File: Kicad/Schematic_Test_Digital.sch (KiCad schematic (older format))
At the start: 72 parts, among them J301 GPS - I2C OUT, J302 SCREEN - I2C OUT, J303 SWD_DEBUG, J304 CONN_JOYSTICK, J305 GENERAL - I2C OUT, SW301 RESET PUSH, U301 TSX-3225, U302 MMC5603NJ, U303 LSM6DS33TR, U304 74HC595PW, U305 74HC595PW, U306 74HC595PW

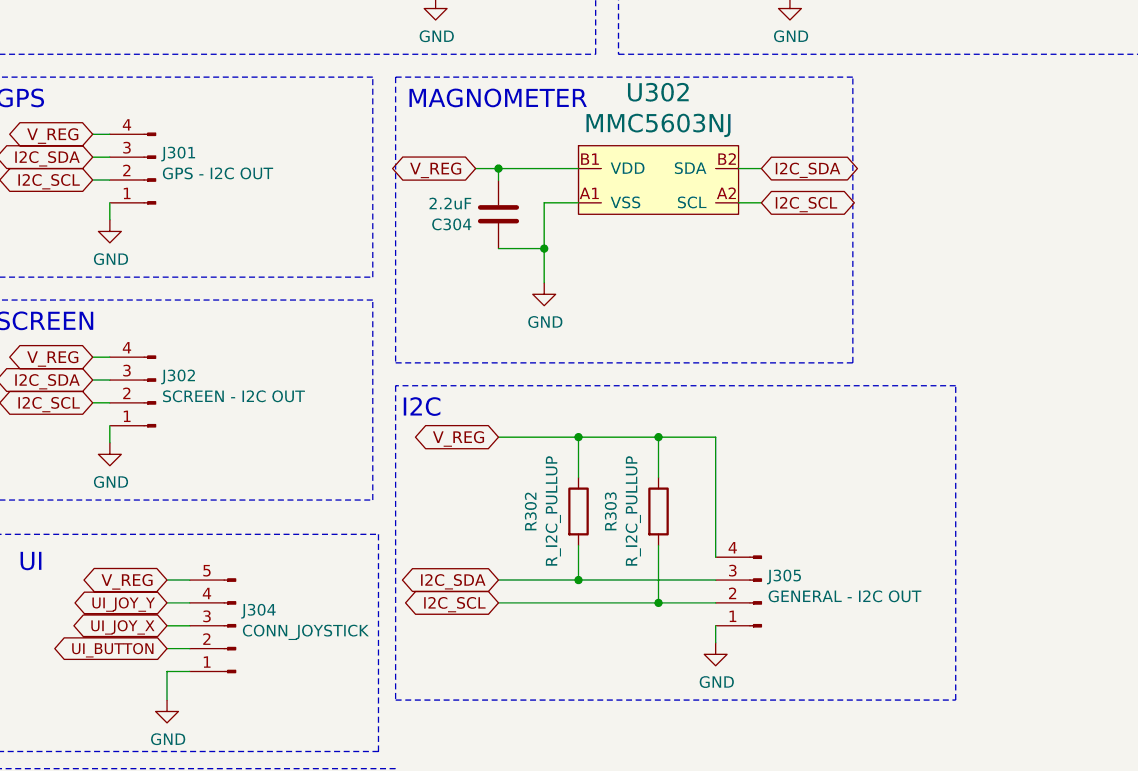
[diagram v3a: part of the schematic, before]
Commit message: "PREVIOUS COMMIT MAIN SCHEMATIC CORRUPTED (???).  Used commit before that."
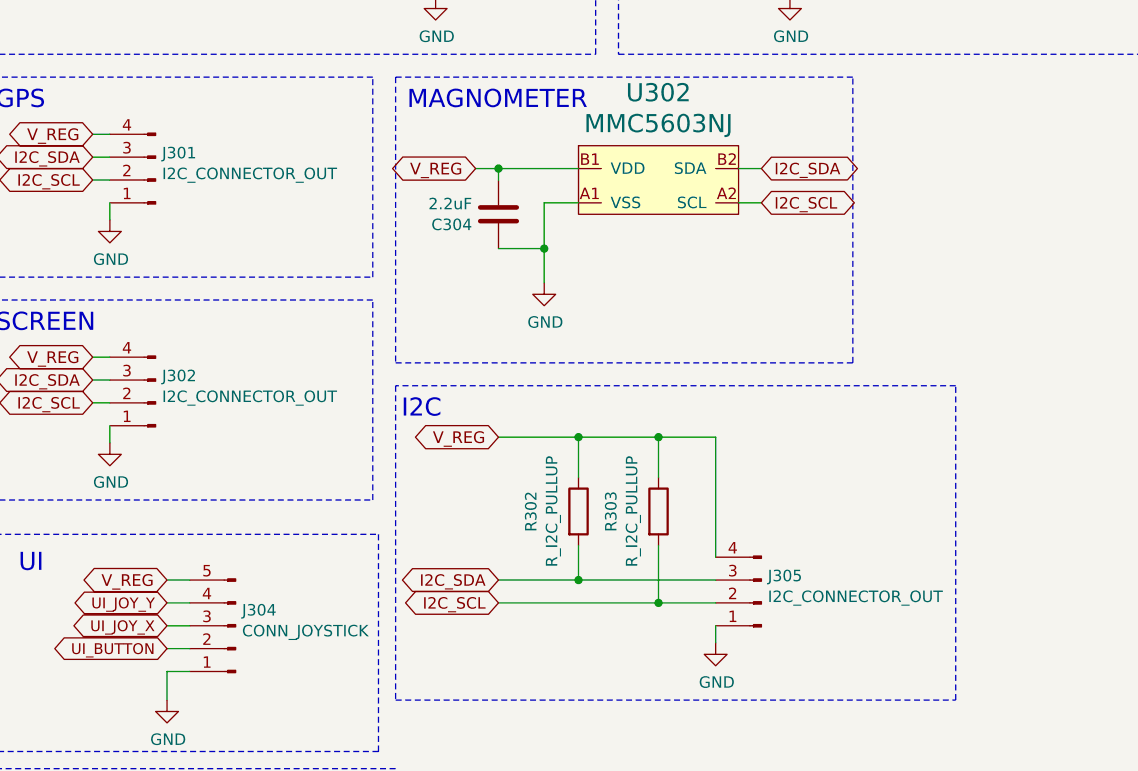
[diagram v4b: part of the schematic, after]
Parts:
- J301: value GPS - I2C OUT -> I2C_CONNECTOR_OUT; part_url (none) -> LOCAL STOCK
- J302: value SCREEN - I2C OUT -> I2C_CONNECTOR_OUT; part_url (none) -> LOCAL STOCK
- J305: value GENERAL - I2C OUT -> I2C_CONNECTOR_OUT; part_url (none) -> LOCAL STOCK
- U304, U305, U306: footprint Package_SO:TSSOP-16_4.4x5mm_P0.65mm -> Package_SO:TSSOP-14_4.4x5mm_P0.65mm
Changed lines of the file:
@@
 AR Path="/5F580392/5F64B2DD" Ref="J302"  Part="1"
 F 0 "J302" H 1272 4932 50  0000 R CNN
-F 1 "SCREEN - I2C OUT" H 1272 5023 50  0000 R CNN
+F 1 "I2C_CONNECTOR_OUT" H 1272 5023 50  0000 R CNN
 F 2 "Connector_JST:JST_EH_B4B-EH-A_1x04_P2.50mm_Vertical" H 1300 5050 50  0001 C CNN
 F 3 "~" H 1300 5050 50  0001 C CNN
 F 4 "JST - 4 pin" H 1300 5050 50  0001 C CNN "part_details"
-F 5 "" H 1300 5050 50  0001 C CNN "part_url"
+F 5 "LOCAL STOCK" H 1300 5050 50  0001 C CNN "part_url"
 	1    1300 5050
 	-1   0    0    1
@@
 AR Path="/5F580392/5F64B2F5" Ref="J301"  Part="1"
 F 0 "J301" H 1272 3957 50  0000 R CNN
-F 1 "GPS - I2C OUT" H 1272 4048 50  0000 R CNN
+F 1 "I2C_CONNECTOR_OUT" H 1272 4048 50  0000 R CNN
 F 2 "Connector_JST:JST_EH_B4B-EH-A_1x04_P2.50mm_Vertical" H 1300 4075 50  0001 C CNN
 F 3 "~" H 1300 4075 50  0001 C CNN
 F 4 "JST - 4 pin" H 1300 4075 50  0001 C CNN "part_details"
-F 5 "" H 1300 4075 50  0001 C CNN "part_url"
+F 5 "LOCAL STOCK" H 1300 4075 50  0001 C CNN "part_url"
 	1    1300 4075
 	-1   0    0    1
@@
 	0    1    1    0
 $EndComp
+Wire Wire Line
+	9550 4200 9900 4200
 Connection ~ 10700 3375
 Wire Wire Line
@@
 AR Path="/5F580392/5F64B4A9" Ref="J305"  Part="1"
 F 0 "J305" H 3922 5807 50  0000 R CNN
-F 1 "GENERAL - I2C OUT" H 3922 5898 50  0000 R CNN
+F 1 "I2C_CONNECTOR_OUT" H 3922 5898 50  0000 R CNN
 F 2 "Connector_JST:JST_EH_B4B-EH-A_1x04_P2.50mm_Vertical" H 3950 5925 50  0001 C CNN
 F 3 "~" H 3950 5925 50  0001 C CNN
 F 4 "JST - 4 pin" H 3950 5925 50  0001 C CNN "part_details"
-F 5 "" H 3950 5925 50  0001 C CNN "part_url"
+F 5 "LOCAL STOCK" H 3950 5925 50  0001 C CNN "part_url"
 	1    3950 5925
 	-1   0    0    1
@@
 	3000 4375 3000 4525
 Connection ~ 3000 4375
+Wire Wire Line
+	2800 4025 3150 4025
+Connection ~ 2800 4025
 Wire Wire Line
 	2700 4025 2800 4025
@@
 	1    0    0    -1
 $EndComp
+Wire Wire Line
+	3150 4175 3000 4175
+Wire Wire Line
+	3950 4175 3850 4175
+Wire Wire Line
+	3950 4025 3850 4025
 $Comp
 L StarGazer:MMC5603NJ U?
@@
 F 0 "U304" H 9125 1092 50  0000 C CNN
 F 1 "74HC595PW" H 9125 1000 51  0000 C CNN
-F 2 "Package_SO:TSSOP-16_4.4x5mm_P0.65mm" H 9200 1125 50  0001 C CNN
+F 2 "Package_SO:TSSOP-14_4.4x5mm_P0.65mm" H 9200 1125 50  0001 C CNN
 F 3 "" H 9200 1125 50  0001 C CNN
 F 4 "Shift Register" H 9150 1025 50  0001 C CNN "part_details"
@@
 F 0 "U306" H 9125 4067 50  0000 C CNN
 F 1 "74HC595PW" H 9125 3975 51  0000 C CNN
-F 2 "Package_SO:TSSOP-16_4.4x5mm_P0.65mm" H 9200 4100 50  0001 C CNN
+F 2 "Package_SO:TSSOP-14_4.4x5mm_P0.65mm" H 9200 4100 50  0001 C CNN
 F 3 "" H 9200 4100 50  0001 C CNN
 F 4 "Shift Register" H 9150 4000 50  0001 C CNN "part_details"
@@
 F 0 "U305" H 9125 2542 50  0000 C CNN
 F 1 "74HC595PW" H 9125 2450 51  0000 C CNN
-F 2 "Package_SO:TSSOP-16_4.4x5mm_P0.65mm" H 9200 2575 50  0001 C CNN
+F 2 "Package_SO:TSSOP-14_4.4x5mm_P0.65mm" H 9200 2575 50  0001 C CNN
 F 3 "" H 9200 2575 50  0001 C CNN
 F 4 "Shift Register" H 9150 2475 50  0001 C CNN "part_details"
@@
 Text Notes 650  6775 0    50   ~ 0
 SWD - PROGRAM\n
-Wire Wire Line
-	9550 4200 9900 4200
-Wire Wire Line
-	2800 4025 3150 4025
-Connection ~ 2800 4025
-Wire Wire Line
-	3000 4175 3150 4175
-Wire Wire Line
-	3950 4175 3850 4175
-Wire Wire Line
-	3850 4025 3950 4025
 $EndSCHEMATC

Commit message: End of night, progress continues.
Parts are getting initial placement.

confidence raises.
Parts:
- U304, U305, U306: footprint Package_SO:TSSOP-14_4.4x5mm_P0.65mm -> Package_SO:TSSOP-16_4.4x5mm_P0.65mm
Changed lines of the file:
@@
 F 0 "U304" H 9125 1092 50  0000 C CNN
 F 1 "74HC595PW" H 9125 1000 51  0000 C CNN
-F 2 "Package_SO:TSSOP-14_4.4x5mm_P0.65mm" H 9200 1125 50  0001 C CNN
+F 2 "Package_SO:TSSOP-16_4.4x5mm_P0.65mm" H 9200 1125 50  0001 C CNN
 F 3 "" H 9200 1125 50  0001 C CNN
 F 4 "Shift Register" H 9150 1025 50  0001 C CNN "part_details"
@@
 F 0 "U306" H 9125 4067 50  0000 C CNN
 F 1 "74HC595PW" H 9125 3975 51  0000 C CNN
-F 2 "Package_SO:TSSOP-14_4.4x5mm_P0.65mm" H 9200 4100 50  0001 C CNN
+F 2 "Package_SO:TSSOP-16_4.4x5mm_P0.65mm" H 9200 4100 50  0001 C CNN
 F 3 "" H 9200 4100 50  0001 C CNN
 F 4 "Shift Register" H 9150 4000 50  0001 C CNN "part_details"
@@
 F 0 "U305" H 9125 2542 50  0000 C CNN
 F 1 "74HC595PW" H 9125 2450 51  0000 C CNN
-F 2 "Package_SO:TSSOP-14_4.4x5mm_P0.65mm" H 9200 2575 50  0001 C CNN
+F 2 "Package_SO:TSSOP-16_4.4x5mm_P0.65mm" H 9200 2575 50  0001 C CNN
 F 3 "" H 9200 2575 50  0001 C CNN
 F 4 "Shift Register" H 9150 2475 50  0001 C CNN "part_details"

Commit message: Updated magnometer to LIS3MDL which has a more sane footprint.
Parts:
- added C309: 100nF, Capacitor_SMD:C_0805_2012Metric_Pad1.15x1.40mm_HandSolder, symbol Device:C
- added C310: 1uF, Capacitor_SMD:CP_Elec_4x3, symbol Device:CP
- C304: value 2.2uF -> 100nF
- U302: value MMC5603NJ -> LIS3MDLTR; footprint Package_BGA:WLP-4_0.73x0.73mm_Layout2x2_P0.35mm_Ball0.22mm_Pad0.2mm_NSMD -> Package_LGA:LGA-12_2x2mm_P0.5mm; symbol StarGazer:MMC5603NJ -> StarGazer:LIS3MDL; part_name MMC5603NJ -> LIS3MDLTR; part_url https://www.digikey.com/product-detail/en/memsic-inc/MMC560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 -> https://www.digikey.com/product-detail/en/stmicroelectronic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
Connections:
- net GND: now also C304.1, U302.12 (RES), U302.2 (RES), U302.3 (GND), C309.1, C310.2; no longer C304.2, U302.A1 (VSS)
- net I2C_SCL: now also U302.1 (SCL/SPC); no longer U302.A2 (SCL)
- net I2C_SDA: now also U302.11 (SDA/SDI/SDO); no longer U302.B2 (SDA)
- net V_REG: now also U302.10 (CS), U302.5 (VDD), U302.6 (VDD_IO), U302.9 (SD0/SA1), C309.2, C310.1; no longer C304.1, U302.B1 (VDD)
- new net: C304.2, U302.4 (C1)
- no-connect marks 3 -> 5

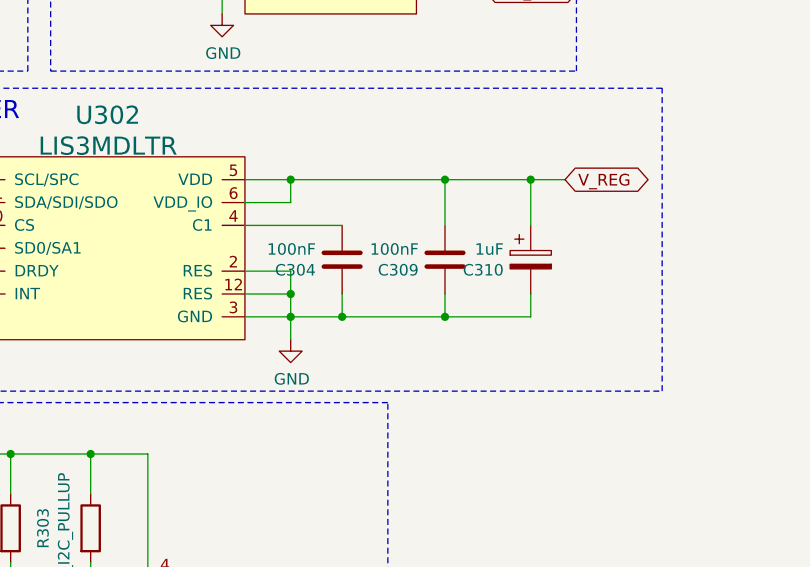
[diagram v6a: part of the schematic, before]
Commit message: Discovered small bug with BoM script.  It does not acccount for all parameters, such as foot print.  This resulted in it thinking a electro-cap could be a ceramic-cap since they shared the same value.
To simplify parts, C310 is now a ceramic cap at the same value.
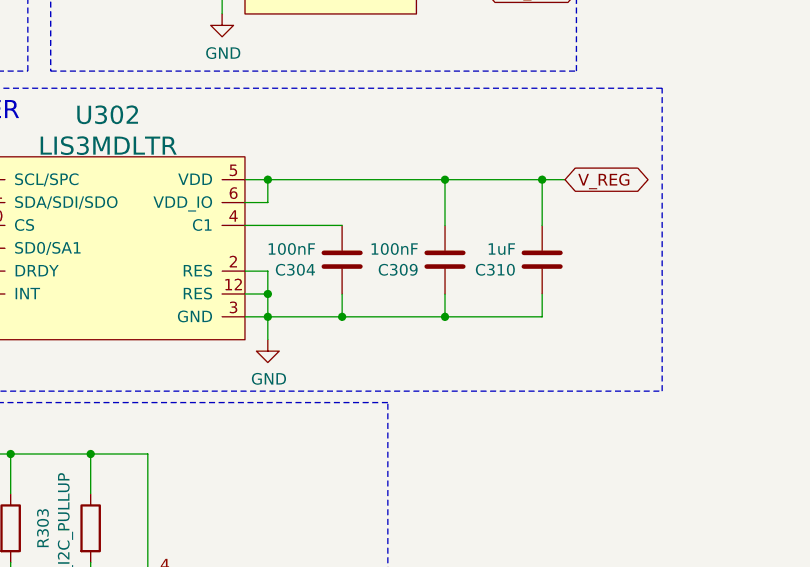
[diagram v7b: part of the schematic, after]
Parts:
- removed C310: 1uF, Capacitor_SMD:CP_Elec_4x3, symbol Device:CP
- added C310: 1uF, Capacitor_SMD:C_0805_2012Metric_Pad1.15x1.40mm_HandSolder, symbol Device:C
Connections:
- net GND: now also C310.1
- net V_REG: now also C310.2
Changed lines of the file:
@@
 L power:GND #PWR0105
 U 1 1 5F746BCA
-P 4375 4700
-F 0 "#PWR0105" H 4375 4450 50  0001 C CNN
-F 1 "GND" H 4380 4527 50  0000 C CNN
-F 2 "" H 4375 4700 50  0001 C CNN
-F 3 "" H 4375 4700 50  0001 C CNN
-	1    4375 4700
+P 4275 4700
+F 0 "#PWR0105" H 4275 4450 50  0001 C CNN
+F 1 "GND" H 4280 4527 50  0000 C CNN
+F 2 "" H 4275 4700 50  0001 C CNN
+F 3 "" H 4275 4700 50  0001 C CNN
+	1    4275 4700
 	1    0    0    -1
 $EndComp
 Wire Wire Line
-	4175 4600 4375 4600
-Wire Wire Line
-	4375 4600 4375 4700
-Connection ~ 4375 4600
-Wire Wire Line
-	4175 4400 4375 4400
+	4175 4600 4275 4600
+Wire Wire Line
+	4275 4600 4275 4700
+Connection ~ 4275 4600
+Wire Wire Line
+	4175 4400 4275 4400
 Wire Wire Line
 	3025 4500 2875 4500
@@
 V_REG
 Wire Wire Line
-	5575 4000 5425 4000
-Wire Wire Line
-	4175 4100 4375 4100
-Wire Wire Line
-	4375 4100 4375 4000
-Connection ~ 4375 4000
-Wire Wire Line
-	4375 4000 4175 4000
+	5575 4000 5475 4000
+Wire Wire Line
+	4175 4100 4275 4100
+Wire Wire Line
+	4275 4100 4275 4000
+Connection ~ 4275 4000
+Wire Wire Line
+	4275 4000 4175 4000
 $Comp
 L Device:C C?
@@
 $EndComp
 Wire Wire Line
-	4375 4000 5050 4000
+	4275 4000 5050 4000
 Wire Wire Line
 	5050 4000 5050 4200
@@
 	4175 4200 4600 4200
 Wire Wire Line
-	4375 4400 4375 4500
-Wire Wire Line
-	4375 4500 4375 4600
-Wire Wire Line
-	4175 4500 4375 4500
+	4275 4400 4275 4500
+Wire Wire Line
+	4275 4500 4275 4600
+Wire Wire Line
+	4175 4500 4275 4500
 $Comp
 L Device:C C?
@@
 	-1   0    0    1
 $EndComp
-Connection ~ 4375 4500
-Wire Wire Line
-	4375 4600 4600 4600
+Connection ~ 4275 4500
+Wire Wire Line
+	4275 4600 4600 4600
 Wire Wire Line
 	5050 4500 5050 4600
@@
 Wire Wire Line
 	4600 4500 4600 4600
-$Comp
-L Device:CP C?
-U 1 1 5FA10C8E
-P 5425 4350
-AR Path="/5FA10C8E" Ref="C?"  Part="1"
-AR Path="/5F580392/5FA10C8E" Ref="C310"  Part="1"
-F 0 "C310" H 5307 4304 50  0000 R CNN
-F 1 "1uF" H 5307 4395 50  0000 R CNN
-F 2 "Capacitor_SMD:CP_Elec_4x3" H 5463 4200 50  0001 C CNN
-F 3 "~" H 5425 4350 50  0001 C CNN
-F 4 "Capactitor - Bypass" H 5425 4350 50  0001 C CNN "part_name"
-F 5 "https://www.digikey.com/product-detail/en/w%C3%BCrth-elektronik/865080340001/732-8411-1-ND/5728368" H 5425 4350 50  0001 C CNN "part_url"
-	1    5425 4350
-	1    0    0    -1
-$EndComp
-Wire Wire Line
-	5425 4500 5425 4600
-Wire Wire Line
-	5425 4600 5050 4600
+Wire Wire Line
+	5475 4500 5475 4600
+Wire Wire Line
+	5475 4600 5050 4600
 Connection ~ 5050 4600
 Wire Wire Line
-	5050 4000 5425 4000
-Wire Wire Line
-	5425 4000 5425 4200
+	5050 4000 5475 4000
+Wire Wire Line
+	5475 4000 5475 4200
 Connection ~ 5050 4000
-Connection ~ 5425 4000
+Connection ~ 5475 4000
 Wire Wire Line
 	3025 4400 2875 4400
@@
 Wire Wire Line
 	10700 2675 10700 2775
+$Comp
+L Device:C C?
+U 1 1 5FC220FB
+P 5475 4350
+AR Path="/5FC220FB" Ref="C?"  Part="1"
+AR Path="/5F580392/5FC220FB" Ref="C310"  Part="1"
+F 0 "C310" H 5590 4396 50  0000 L CNN
+F 1 "1uF" H 5590 4305 50  0000 L CNN
+F 2 "Capacitor_SMD:C_0805_2012Metric_Pad1.15x1.40mm_HandSolder" H 5513 4200 50  0001 C CNN
+F 3 "~" H 5475 4350 50  0001 C CNN
+F 4 "https://www.digikey.com/product-detail/en/w%C3%BCrth-elektronik/885012107001/732-7612-1-ND/5454239" H 5475 4350 50  0001 C CNN "part_url"
+F 5 "Capactitor - Bypass" H 5475 4350 50  0001 C CNN "part_name"
+	1    5475 4350
+	-1   0    0    1
+$EndComp
 $EndSCHEMATC

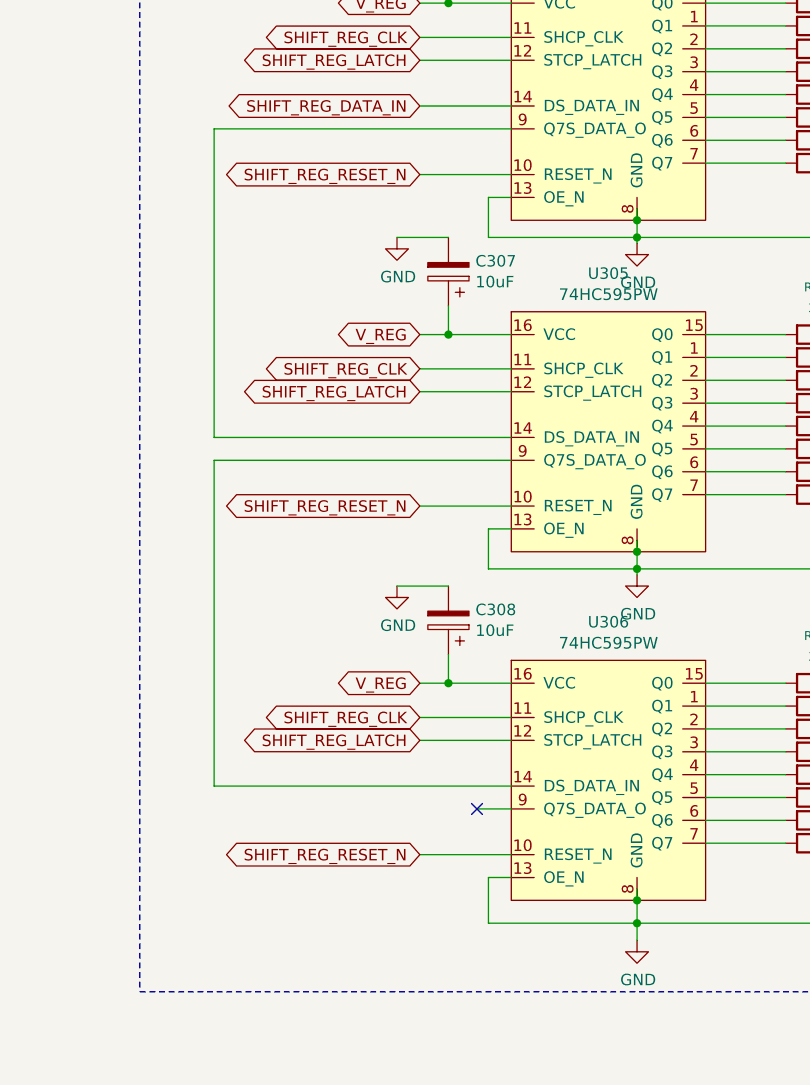
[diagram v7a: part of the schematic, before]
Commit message: Center LED ring laid out and connected. Other components will begin to be fitted into place. Silk screen has not been touched.
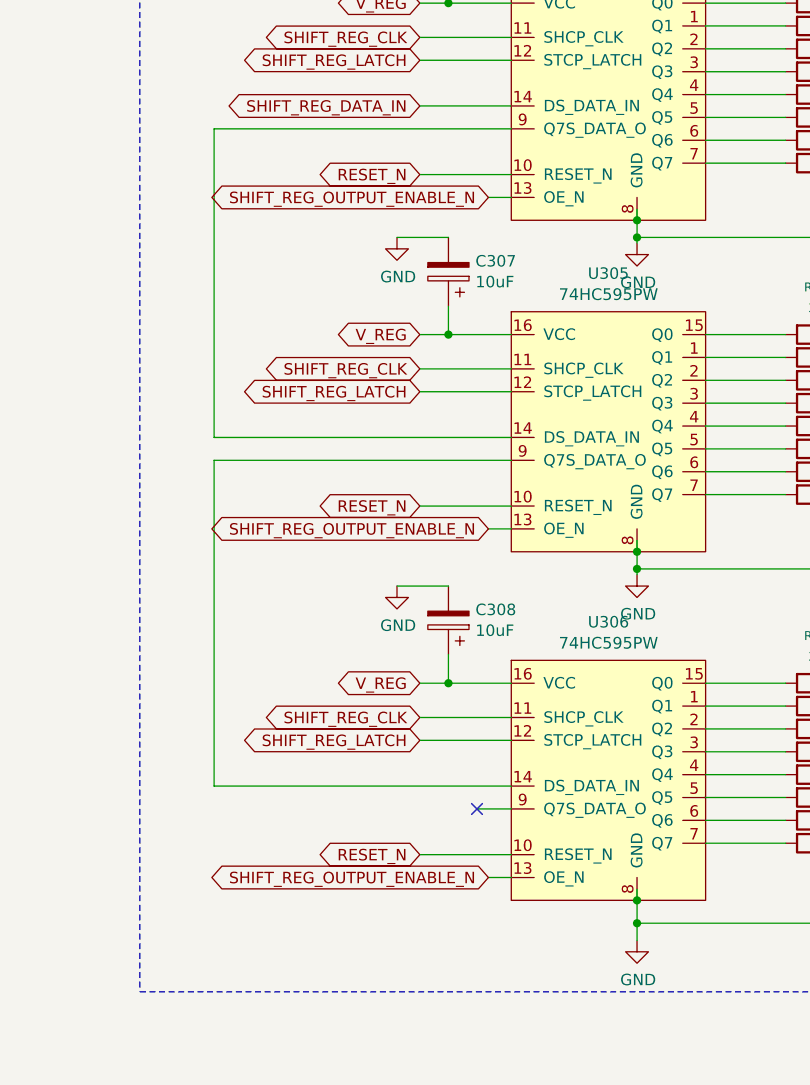
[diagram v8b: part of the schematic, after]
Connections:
- net SHIFT_REG_RESET_N is gone; now on net RESET_N: U304.10 (RESET_N), U305.10 (RESET_N), U306.10 (RESET_N)
- net GND: no longer U304.13 (OE_N), U305.13 (OE_N), U306.13 (OE_N)
- new net SHIFT_REG_OUTPUT_ENABLE_N: U304.13 (OE_N), U305.13 (OE_N), U306.13 (OE_N)
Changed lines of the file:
@@
 Connection ~ 9250 5250
-Wire Wire Line
-	8600 5250 9250 5250
-Wire Wire Line
-	8600 5050 8600 5250
 Wire Wire Line
 	8700 5050 8600 5050
@@
 Connection ~ 9250 3700
 Wire Wire Line
-	8600 3700 9250 3700
-Wire Wire Line
-	8600 3525 8600 3700
-Wire Wire Line
 	8700 3525 8600 3525
 Text GLabel 8300 2925 0    50   BiDi ~ 0
@@
 Text GLabel 1225 1325 0    50   BiDi ~ 0
 RESET_N
-Text GLabel 8300 3425 0    50   BiDi ~ 0
-SHIFT_REG_RESET_N
-Text GLabel 8300 4950 0    50   BiDi ~ 0
-SHIFT_REG_RESET_N
+Text GLabel 8600 3525 0    50   BiDi ~ 0
+SHIFT_REG_OUTPUT_ENABLE_N
+Text GLabel 8600 5050 0    50   BiDi ~ 0
+SHIFT_REG_OUTPUT_ENABLE_N
 Wire Wire Line
 	8700 4750 8550 4750
@@
 Text GLabel 8300 1675 0    50   BiDi ~ 0
 SHIFT_REG_DATA_IN
-Text GLabel 8300 1975 0    50   BiDi ~ 0
-SHIFT_REG_RESET_N
+Text GLabel 8600 2075 0    50   BiDi ~ 0
+SHIFT_REG_OUTPUT_ENABLE_N
 $Comp
 L power:GND #PWR?
@@
 	1    0    0    -1
 $EndComp
-Wire Wire Line
-	8600 2075 8600 2250
-Wire Wire Line
-	8600 2250 9250 2250
 Connection ~ 9250 2250
 Wire Wire Line
@@
 	-1   0    0    1
 $EndComp
+Text GLabel 8300 1975 0    50   BiDi ~ 0
+RESET_N
+Text GLabel 8300 4950 0    50   BiDi ~ 0
+RESET_N
+Text GLabel 8300 3425 0    50   BiDi ~ 0
+RESET_N
 $EndSCHEMATC
